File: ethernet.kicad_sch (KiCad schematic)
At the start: 57 parts, among them IC1 RTL8305NB-VC-CG, Y2 X322525MOB4SI

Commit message: mostly done except for RTL8305 power stuff
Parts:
- removed TP1, TP2: TestPoint, TestPoint:TestPoint_Pad_D1.0mm, symbol Connector:TestPoint
- D2, D3, D4, D5, RJ1, RJ2, RJ3, RJ4: now left out of the parts list
- R7: value 270 -> 510
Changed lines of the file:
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@@
 		(unit 1)
 		(exclude_from_sim no)
-		(in_bom yes)
+		(in_bom no)
 		(on_board yes)
 		(dnp yes)
@@
 	)
 	(symbol
-		(lib_id "Connector:TestPoint")
-		(at 71.12 180.34 90)
-		(unit 1)
-		(exclude_from_sim no)
-		(in_bom yes)
-		(on_board yes)
-		(dnp no)
-		(property "Reference" "TP1"
-			(at 64.77 180.34 90)
-			(effects
-				(font
-					(size 1.27 1.27)
-				)
-			)
-		)
-		(property "Value" "TestPoint"
-			(at 64.008 194.056 0)
-			(effects
-				(font
-					(size 1.27 1.27)
-				)
-				(hide yes)
-			)
-		)
-		(property "Footprint" "TestPoint:TestPoint_Pad_D1.0mm"
-			(at 71.12 175.26 0)
-			(effects
-				(font
-					(size 1.27 1.27)
-				)
-				(hide yes)
-			)
-		)
-		(property "Datasheet" "~"
-			(at 71.12 175.26 0)
-			(effects
-				(font
-					(size 1.27 1.27)
-				)
-				(hide yes)
-			)
-		)
-		(property "Description" "test point"
-			(at 71.12 180.34 0)
-			(effects
-				(font
-					(size 1.27 1.27)
-				)
-				(hide yes)
-			)
-		)
-		(pin "1"
-		)
-		(instances
-			(project ""
-				(path "/ebd96e19-6f65-4022-a6da-be26c0716f8e/76b1a870-e345-41cc-887f-c3b81be4cbe1"
-					(reference "TP1")
-					(unit 1)
-				)
-			)
-		)
-	)
-	(symbol
 		(lib_id "power:GND")
 		(at 398.78 100.33 0)
@@
 		(unit 1)
 		(exclude_from_sim no)
-		(in_bom yes)
+		(in_bom no)
 		(on_board yes)
 		(dnp yes)
@@
 		(unit 1)
 		(exclude_from_sim no)
-		(in_bom yes)
+		(in_bom no)
 		(on_board yes)
 		(dnp yes)
@@
 		(unit 1)
 		(exclude_from_sim no)
-		(in_bom yes)
+		(in_bom no)
 		(on_board yes)
 		(dnp yes)
@@
 	)
 	(symbol
-		(lib_id "Connector:TestPoint")
-		(at 71.12 182.88 90)
-		(mirror x)
-		(unit 1)
-		(exclude_from_sim no)
-		(in_bom yes)
-		(on_board yes)
-		(dnp no)
-		(property "Reference" "TP2"
-			(at 64.77 182.88 90)
-			(effects
-				(font
-					(size 1.27 1.27)
-				)
-			)
-		)
-		(property "Value" "TestPoint"
-			(at 58.166 184.912 0)
-			(effects
-				(font
-					(size 1.27 1.27)
-				)
-				(hide yes)
-			)
-		)
-		(property "Footprint" "TestPoint:TestPoint_Pad_D1.0mm"
-			(at 71.12 187.96 0)
-			(effects
-				(font
-					(size 1.27 1.27)
-				)
-				(hide yes)
-			)
-		)
-		(property "Datasheet" "~"
-			(at 71.12 187.96 0)
-			(effects
-				(font
-					(size 1.27 1.27)
-				)
-				(hide yes)
-			)
-		)
-		(property "Description" "test point"
-			(at 71.12 182.88 0)
-			(effects
-				(font
-					(size 1.27 1.27)
-				)
-				(hide yes)
-			)
-		)
-		(pin "1"
-		)
-		(instances
-			(project ""
-				(path "/ebd96e19-6f65-4022-a6da-be26c0716f8e/76b1a870-e345-41cc-887f-c3b81be4cbe1"
-					(reference "TP2")
-					(unit 1)
-				)
-			)
-		)
-	)
-	(symbol
 		(lib_id "power:GND")
 		(at 398.78 166.37 0)
@@
 		(unit 1)
 		(exclude_from_sim no)
-		(in_bom yes)
+		(in_bom no)
 		(on_board yes)
 		(dnp yes)
@@
 		(unit 1)
 		(exclude_from_sim no)
-		(in_bom yes)
+		(in_bom no)
 		(on_board yes)
 		(dnp yes)
@@
 			)
 		)
-		(property "Value" "270"
+		(property "Value" "510"
 			(at 55.88 167.64 90)
 			(effects
@@
 		(unit 1)
 		(exclude_from_sim no)
-		(in_bom yes)
+		(in_bom no)
 		(on_board yes)
 		(dnp yes)
@@
 		(unit 1)
 		(exclude_from_sim no)
-		(in_bom yes)
+		(in_bom no)
 		(on_board yes)
 		(dnp yes)

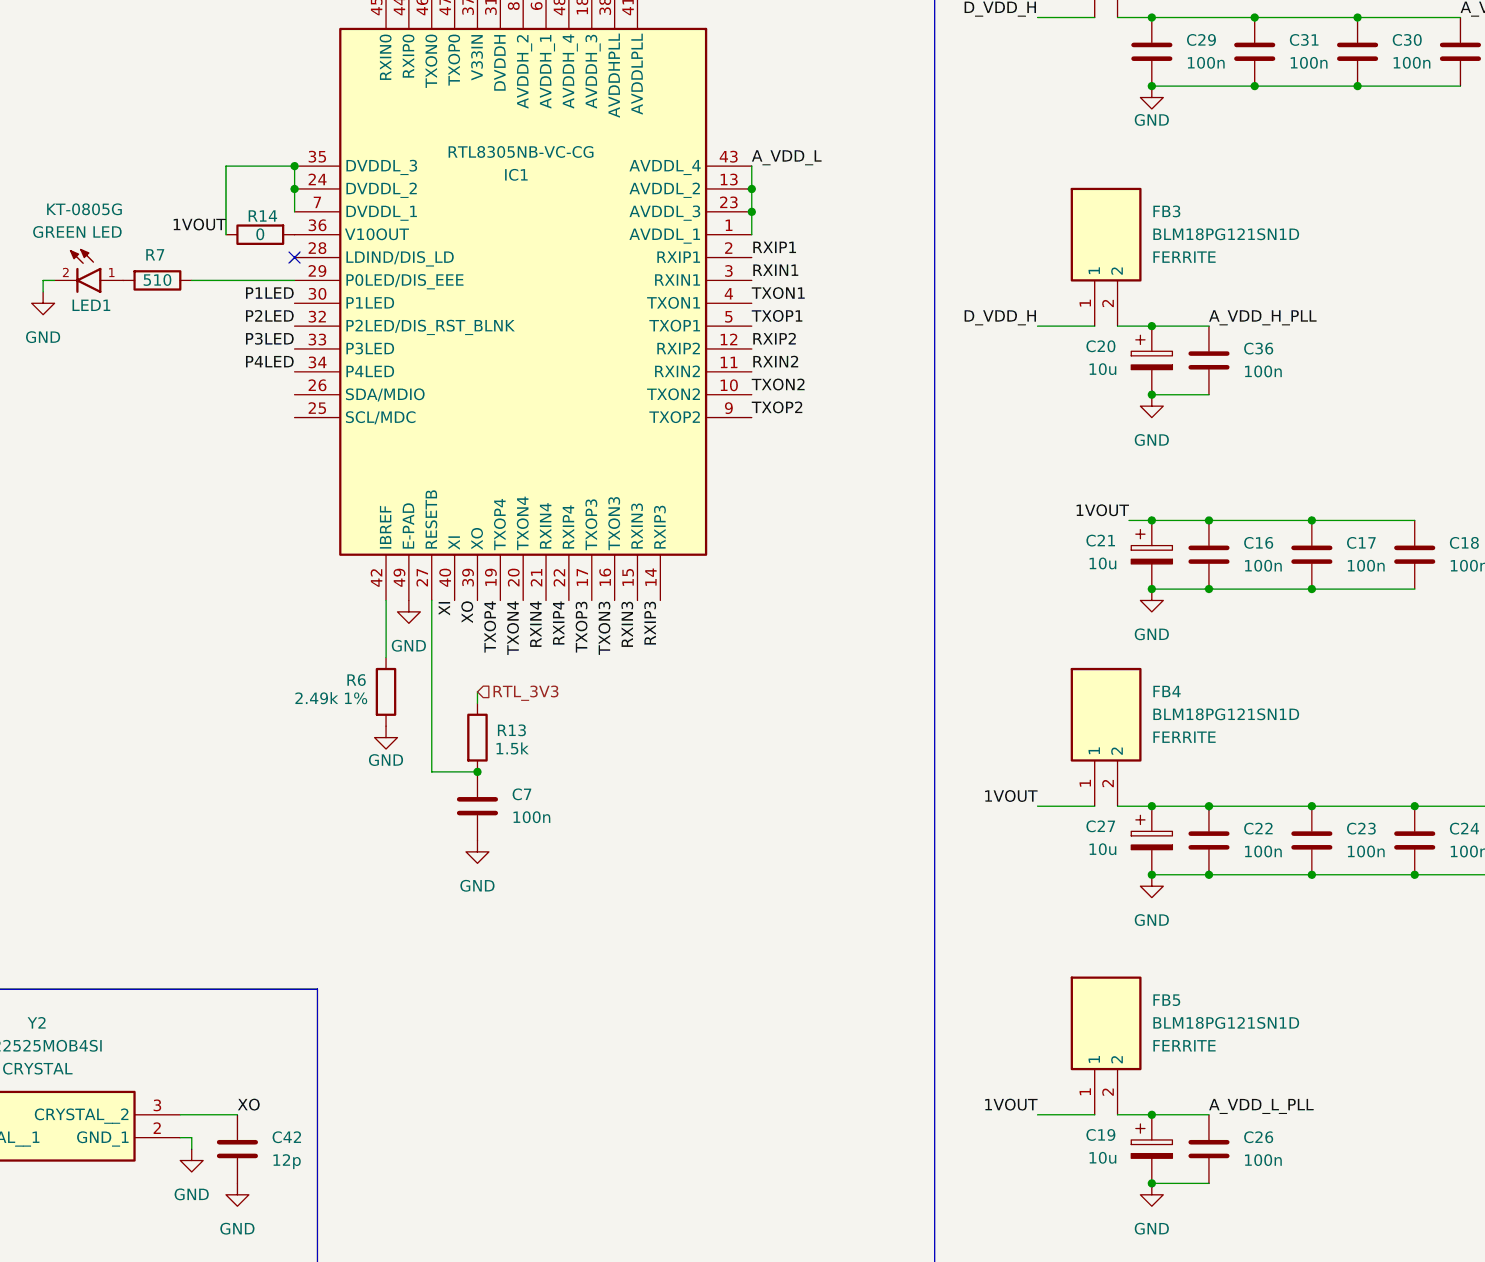
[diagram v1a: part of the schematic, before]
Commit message: most traces complete. need to connect grounds
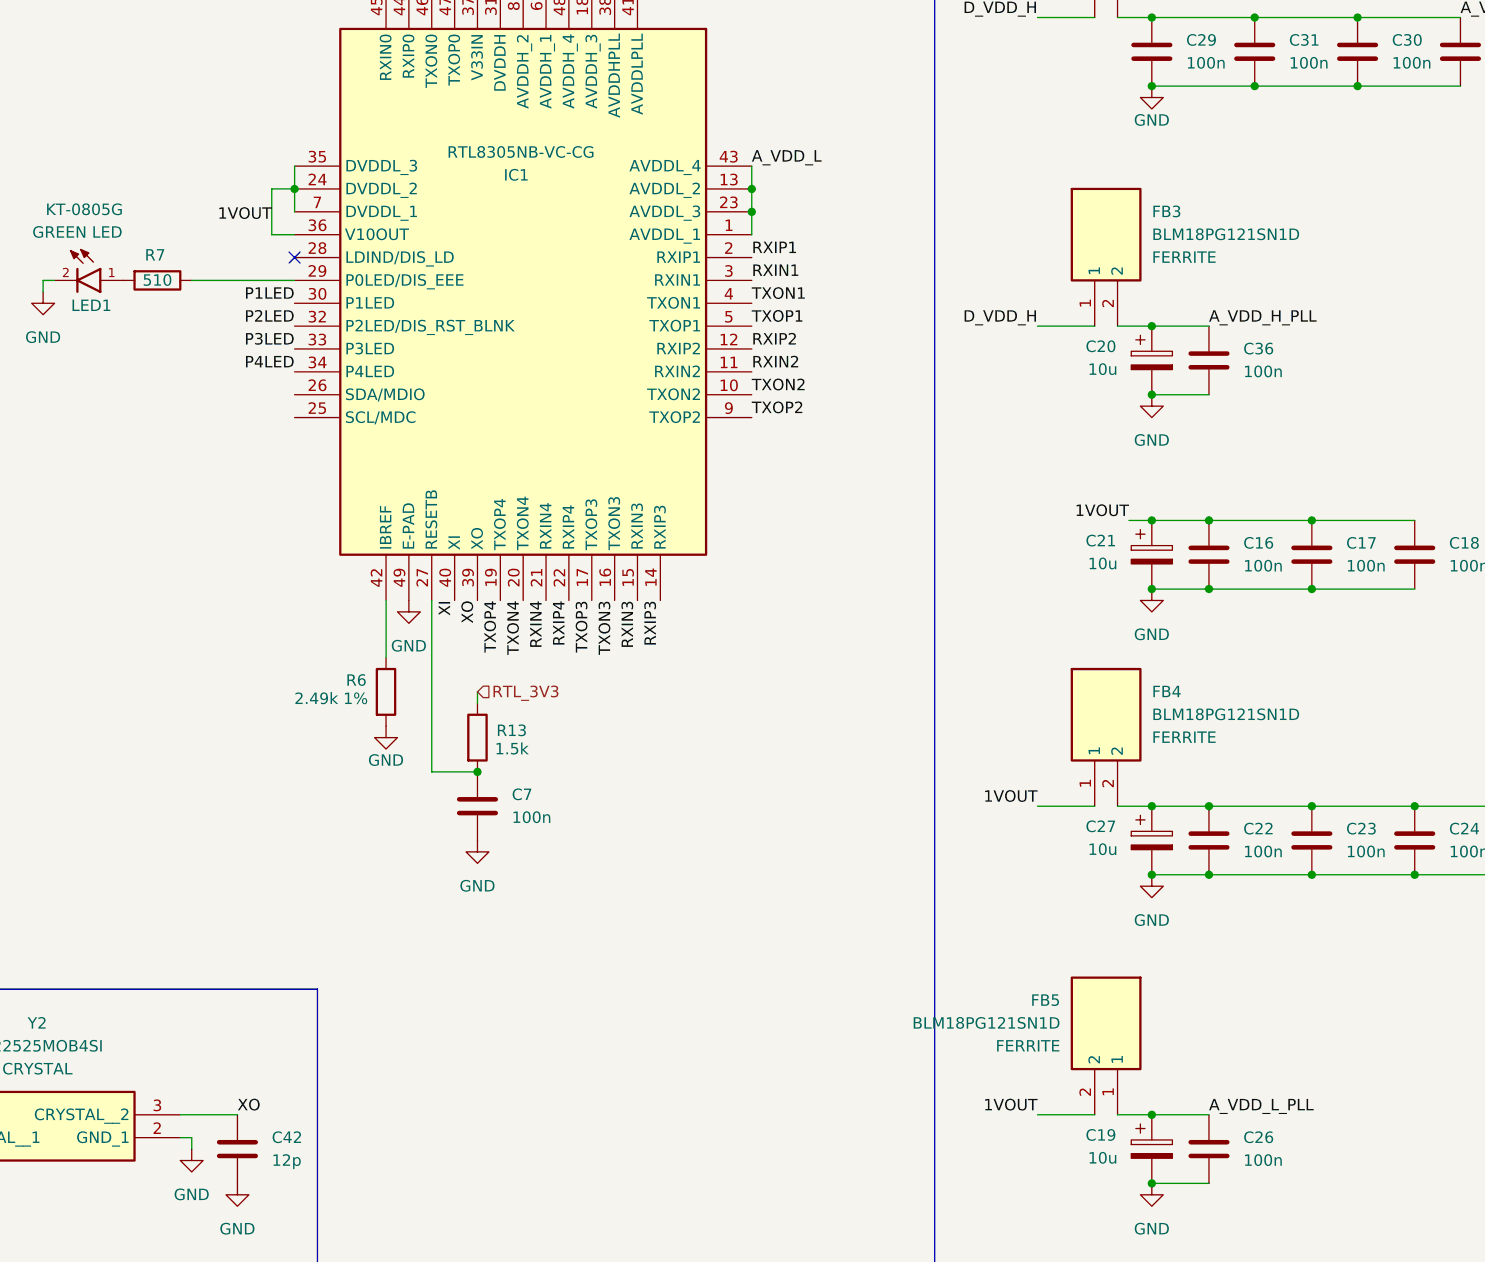
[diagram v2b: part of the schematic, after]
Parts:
- removed R14: 0, Resistor_SMD:R_0402_1005Metric, symbol Device:R
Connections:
- net 1VOUT: now also FB5.2, IC1.36 (V10OUT); no longer FB5.1
- net A_VDD_L_PLL: now also FB5.1; no longer FB5.2
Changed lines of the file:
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@@
 	)
 	(junction
-		(at 71.12 154.94)
-		(diameter 0)
-		(color 0 0 0 0)
-	)
-	(junction
 		(at 166.37 233.68)
 		(diameter 0)
@@
 	(wire
 		(pts
+			(xy 68.58 162.56) (xy 71.12 162.56)
+		)
+		(stroke
+			(width 0)
+			(type default)
+		)
+	)
+	(wire
+		(pts
 			(xy 398.78 99.06) (xy 398.78 96.52)
 		)
@@
 	(wire
 		(pts
-			(xy 71.12 154.94) (xy 71.12 157.48)
+			(xy 316.23 96.52) (xy 314.96 96.52)
 		)
 		(stroke
@@
 	(wire
 		(pts
-			(xy 316.23 96.52) (xy 314.96 96.52)
+			(xy 251.46 86.36) (xy 246.38 86.36)
 		)
 		(stroke
@@
 	(wire
 		(pts
-			(xy 251.46 86.36) (xy 246.38 86.36)
+			(xy 246.38 152.4) (xy 246.38 154.94)
 		)
 		(stroke
@@
 	(wire
 		(pts
-			(xy 246.38 152.4) (xy 246.38 154.94)
+			(xy 71.12 157.48) (xy 71.12 154.94)
 		)
 		(stroke
@@
 	(wire
 		(pts
-			(xy 63.5 154.94) (xy 71.12 154.94)
+			(xy 68.58 157.48) (xy 71.12 157.48)
 		)
 		(stroke
@@
 	(wire
 		(pts
-			(xy 63.5 162.56) (xy 63.5 154.94)
+			(xy 68.58 162.56) (xy 68.58 157.48)
 		)
 		(stroke
@@
 	)
 	(label "1VOUT"
-		(at 63.5 162.56 180)
+		(at 68.58 161.29 180)
 		(effects
 			(font
@@
 	)
 	(symbol
-		(lib_id "Device:R")
-		(at 67.31 162.56 90)
-		(mirror x)
-		(unit 1)
-		(exclude_from_sim no)
-		(in_bom yes)
-		(on_board yes)
-		(dnp no)
-		(property "Reference" "R14"
-			(at 67.564 160.528 90)
-			(effects
-				(font
-					(size 1.27 1.27)
-				)
-			)
-		)
-		(property "Value" "0"
-			(at 67.31 162.56 90)
-			(effects
-				(font
-					(size 1.27 1.27)
-				)
-			)
-		)
-		(property "Footprint" "Resistor_SMD:R_0402_1005Metric"
-			(at 67.31 160.782 90)
-			(effects
-				(font
-					(size 1.27 1.27)
-				)
-				(hide yes)
-			)
-		)
-		(property "Datasheet" "~"
-			(at 67.31 162.56 0)
-			(effects
-				(font
-					(size 1.27 1.27)
-				)
-				(hide yes)
-			)
-		)
-		(property "Description" "Resistor"
-			(at 67.31 162.56 0)
-			(effects
-				(font
-					(size 1.27 1.27)
-				)
-				(hide yes)
-			)
-		)
-		(pin "2"
-		)
-		(pin "1"
-		)
-		(instances
-			(project ""
-				(path "/ebd96e19-6f65-4022-a6da-be26c0716f8e/76b1a870-e345-41cc-887f-c3b81be4cbe1"
-					(reference "R14")
-					(unit 1)
-				)
-			)
-		)
-	)
-	(symbol
 		(lib_id "Device:C_Polarized")
 		(at 166.37 107.95 0)
@@
 		(lib_id "LTELink:FERRITE")
 		(at 161.29 255.27 0)
+		(mirror y)
 		(unit 1)
 		(exclude_from_sim no)
@@
 		(on_board yes)
 		(dnp no)
-		(fields_autoplaced yes)
 		(property "Reference" "FB5"
-			(at 166.37 247.6499 0)
+			(at 156.21 247.6499 0)
 			(effects
 				(font
@@
 		)
 		(property "Value" "BLM18PG121SN1D"
-			(at 166.37 250.1899 0)
+			(at 156.21 250.1899 0)
 			(effects
 				(font
@@
 		)
 		(property "Footprint" "Inductor_SMD:L_0603_1608Metric"
-			(at 177.8 350.19 0)
+			(at 144.78 350.19 0)
 			(effects
 				(font
@@
 		)
 		(property "Datasheet" "https://jlcpcb.com/api/file/downloadByFileSystemAccessId/8588900229559300096"
-			(at 177.8 450.19 0)
+			(at 144.78 450.19 0)
 			(effects
 				(font
@@
 		)
 		(property "Name" "FERRITE"
-			(at 166.37 252.7299 0)
+			(at 156.21 252.7299 0)
 			(effects
 				(font

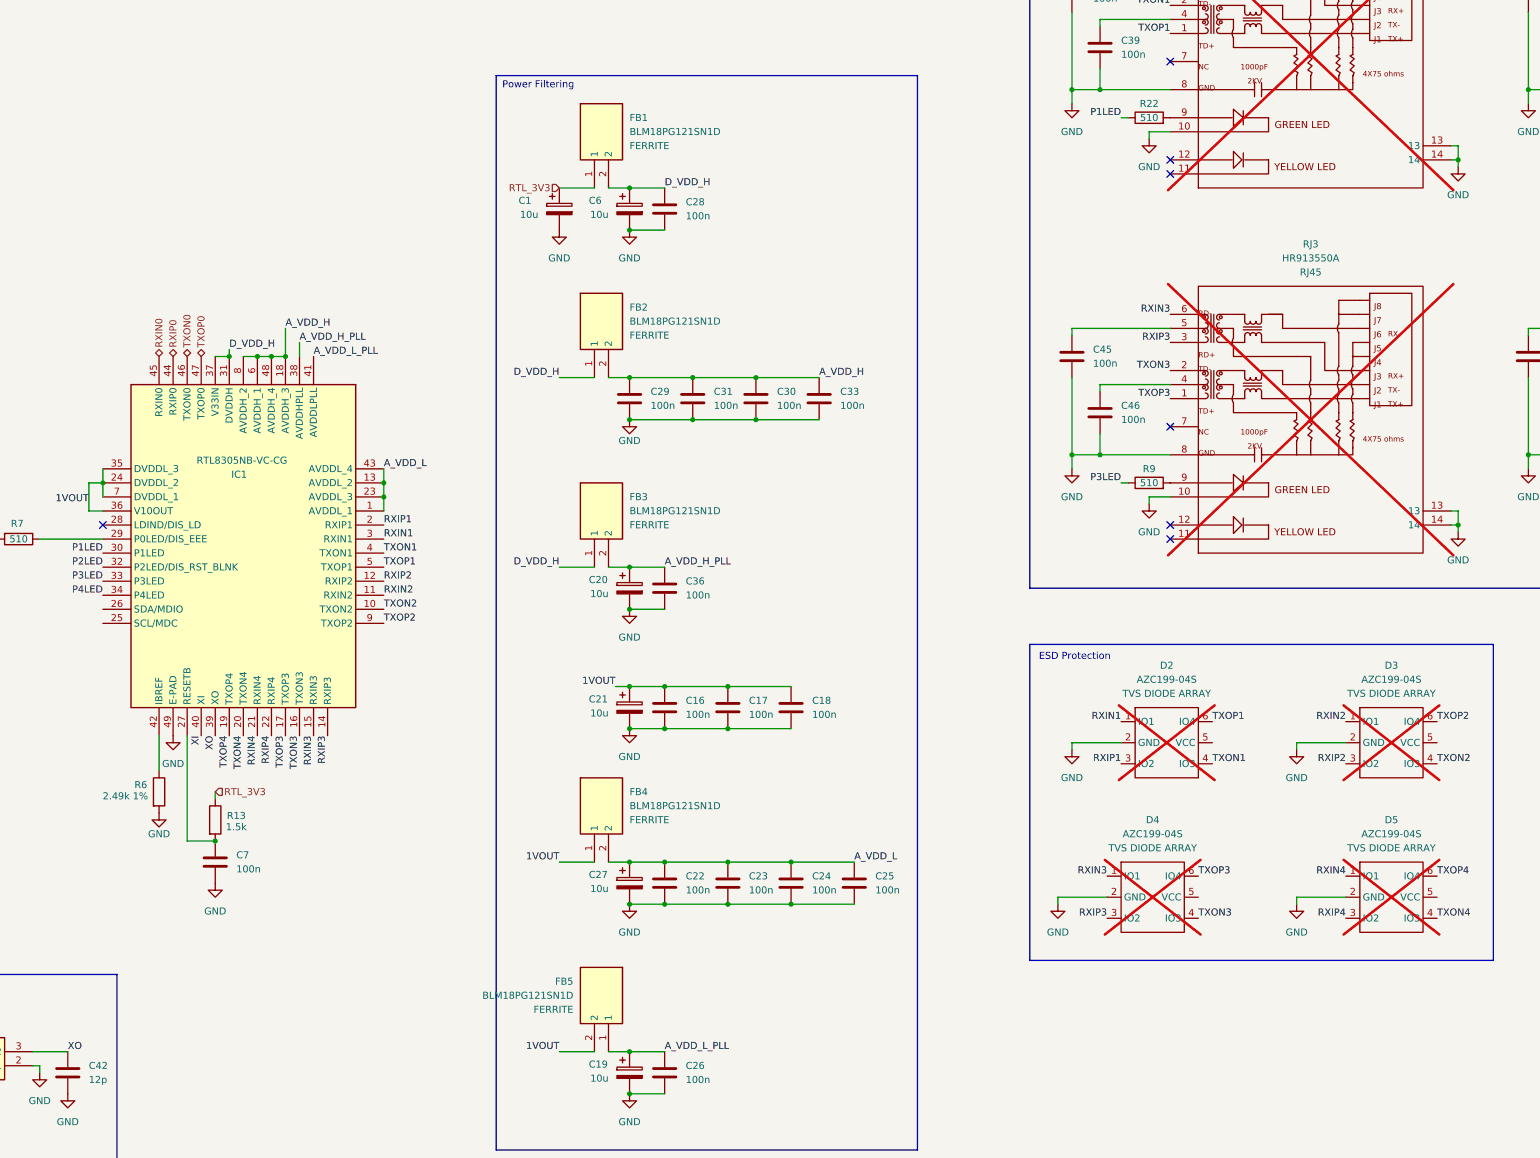
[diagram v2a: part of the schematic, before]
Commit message: replaced ferrites with 0 omh resitors, finalized standoff solution
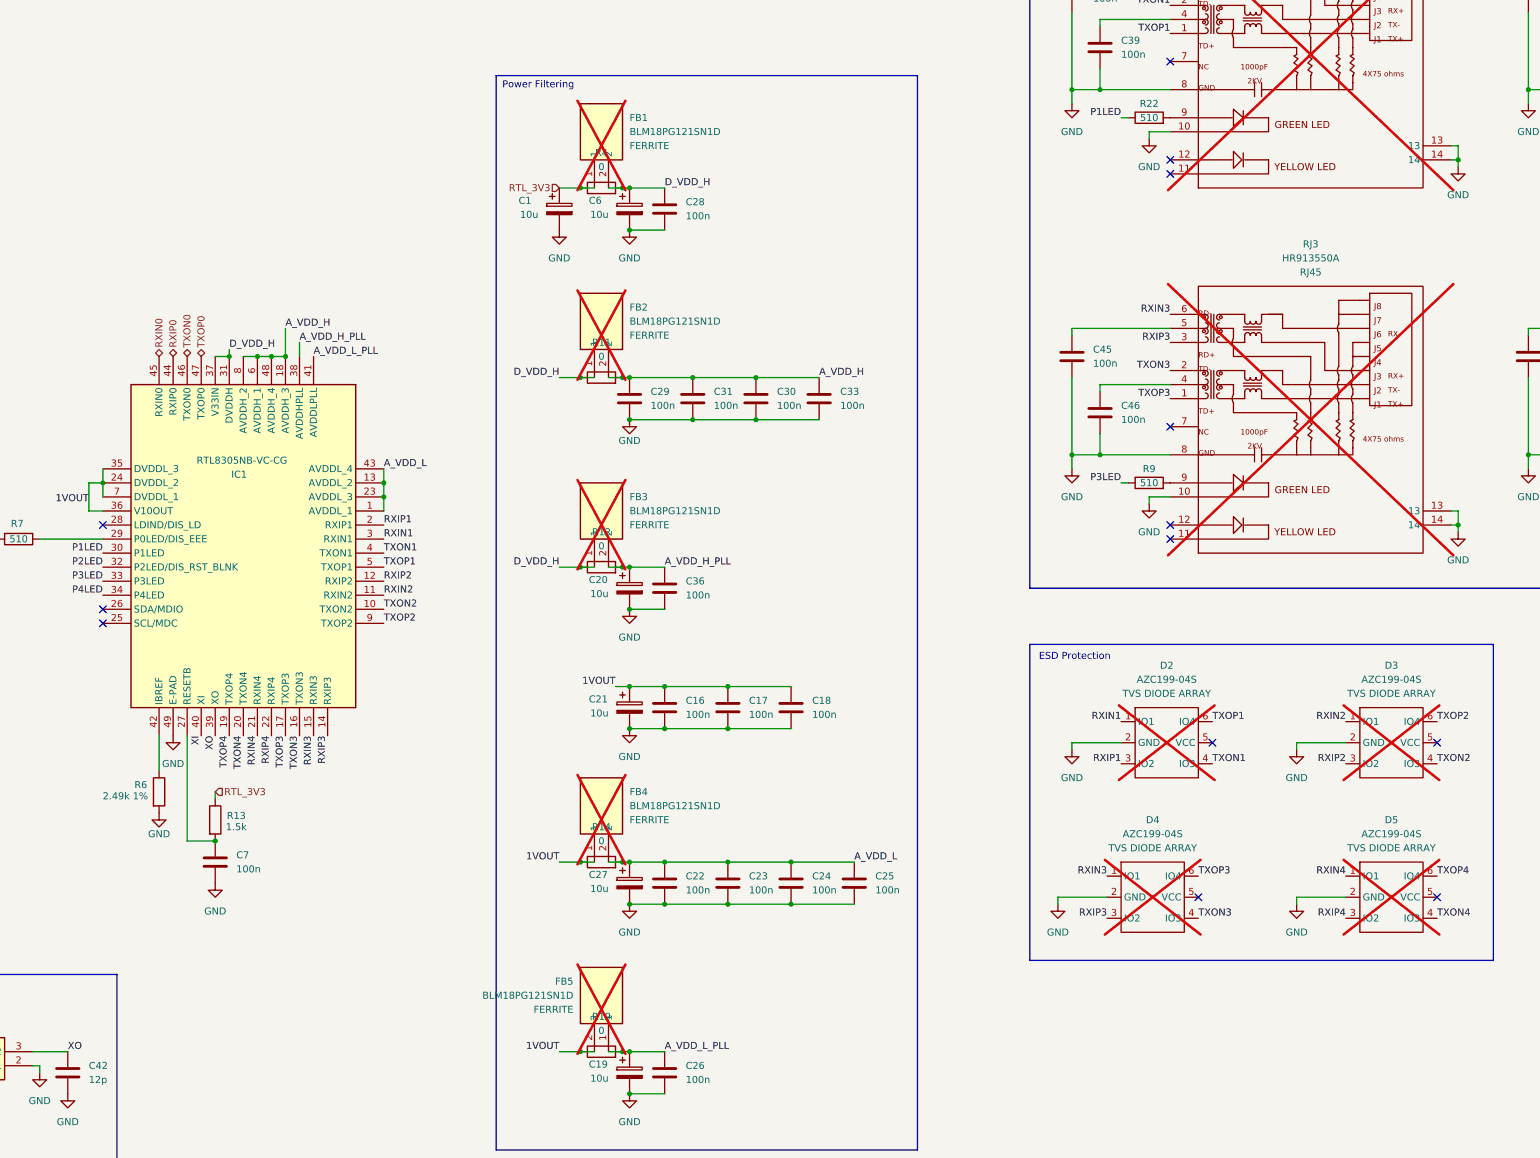
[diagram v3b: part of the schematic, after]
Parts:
- added R11, R12, R14, R19, R4: 0, Resistor_SMD:R_0603_1608Metric, symbol Device:R
- FB1, FB2, FB3, FB4, FB5: now not fitted; now left out of the parts list
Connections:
- net 1VOUT: now also R14.1, R19.1
- net A_VDD_H: now also R11.2
- net A_VDD_H_PLL: now also R12.2
- net A_VDD_L: now also R14.2
- net A_VDD_L_PLL: now also R19.2
- net D_VDD_H: now also R11.1, R12.1, R4.2
- net RTL_3V3: now also R4.1
- no-connect marks 13 -> 19
